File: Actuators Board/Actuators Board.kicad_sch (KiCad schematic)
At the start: 66 parts, among them IC1 BD62120AEFJ-E2, J1 Conn_01x05_Male, J10 Conn_01x02_Male, J2 Solenoid(Sol), J4 Conn_01x03_Male, J5 Conn_01x06_Male, J9 Conn_01x02_Male, Q1 MMDT2222A, Q2 SI2366DS, U1 ESP32-PICO-D4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

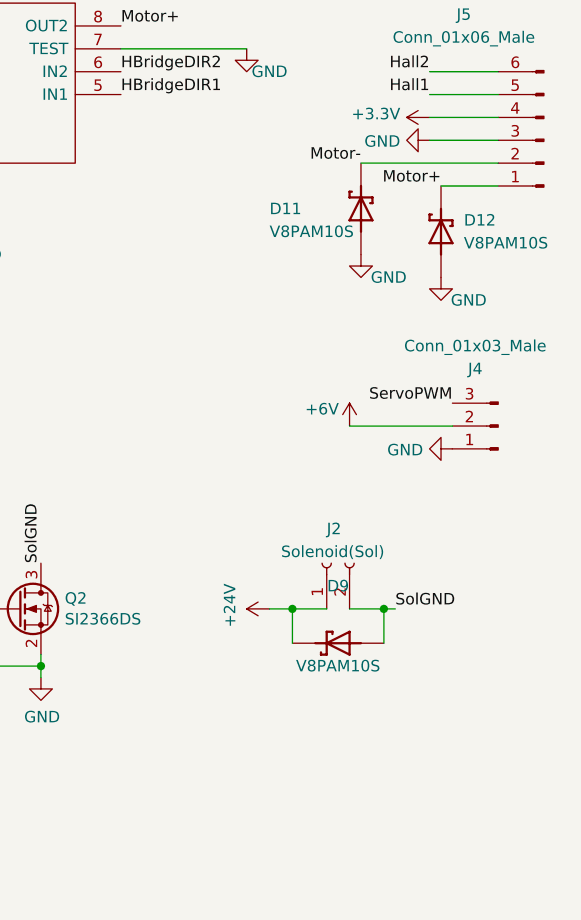
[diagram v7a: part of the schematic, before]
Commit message: Removed more unnecessary files
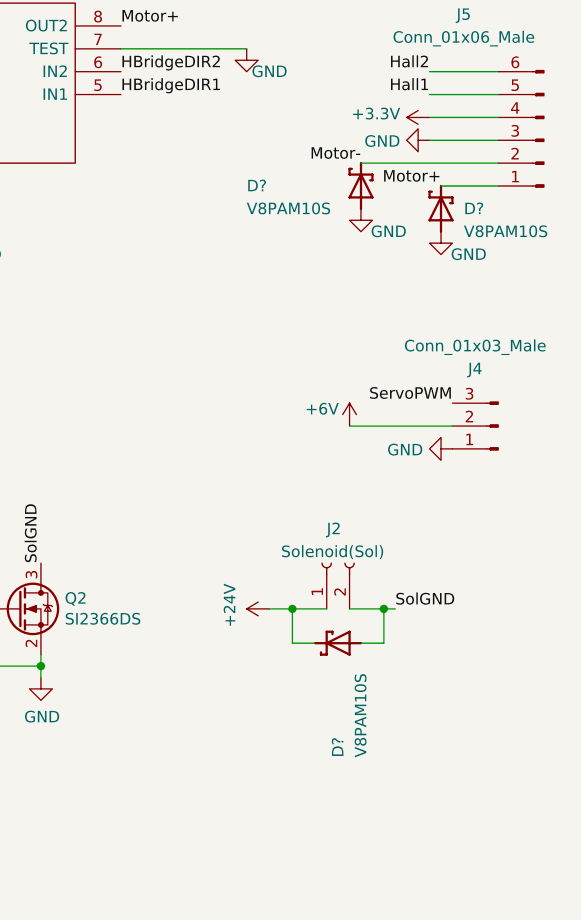
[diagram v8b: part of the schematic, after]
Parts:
- removed D11, D12, D9: V8PAM10S, iclr:DIO_V3PAN50-M3_I, symbol iclr:V3PAN50-M3{brace}slash}I
- added D? (x3): V8PAM10S, DIO_V3PAN50-M3/I, symbol iclr:V8PAM10S
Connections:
- net +24V: now also D?.C
- net GND: now also D?.A, D?.A
- net Motor+: now also D?.C
- net Motor-: now also D?.C
- net SolGND: now also D?.A
